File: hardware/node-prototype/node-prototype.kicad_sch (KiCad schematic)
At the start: 0 parts

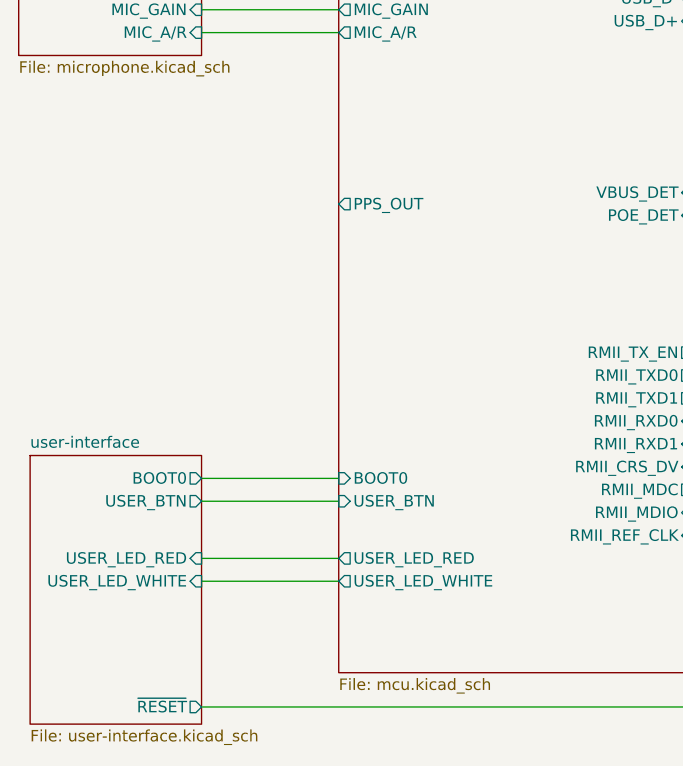
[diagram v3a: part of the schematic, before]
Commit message: Design PPS output, fix LEDs and their resistors
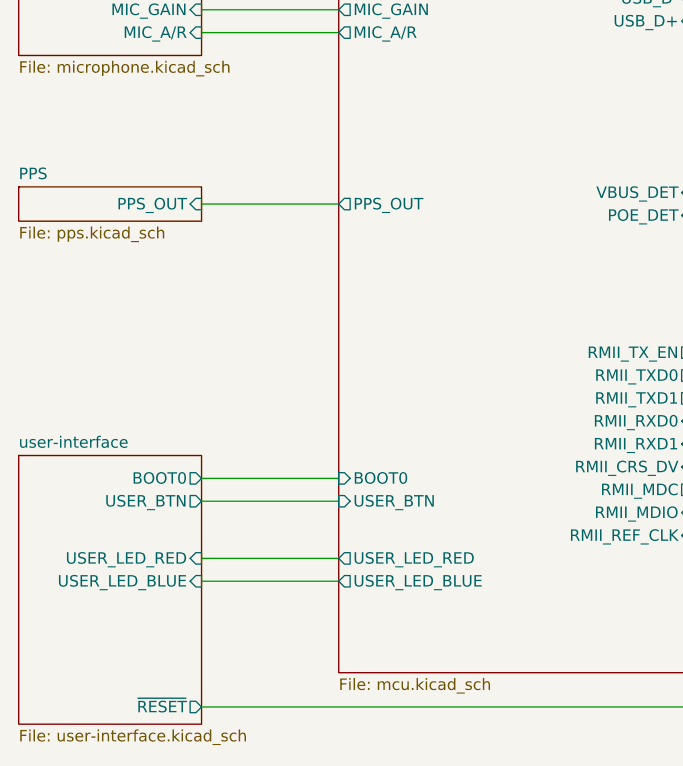
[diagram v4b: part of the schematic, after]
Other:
- added sheet PPS (pps.kicad_sch)
- sheet mcu ports: added USER_LED_BLUE; removed USER_LED_WHITE
- sheet user-interface ports: added USER_LED_BLUE; removed USER_LED_WHITE
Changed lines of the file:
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@@
+    (stroke (width 0) (type default))
+  )
+  (wire (pts (xy 82.55 76.2) (xy 97.79 76.2))
     (stroke (width 0) (type default))
   )
@@
     (effects (font (size 1.27 1.27)) (justify left bottom))
   )
-  (sheet (at 63.5 104.14) (size 19.05 29.845) (fields_autoplaced)
-    (stroke (width 0.1524) (type solid))
-    (fill (color 0 0 0 0.0000))
-    (property "Sheetname" "user-interface" (at 63.5 103.4284 0)
-      (effects (font (size 1.27 1.27)) (justify left bottom))
-    )
-    (property "Sheetfile" "user-interface.kicad_sch" (at 63.5 134.5696 0)
+  (sheet (at 62.23 104.14) (size 20.32 29.845) (fields_autoplaced)
+    (stroke (width 0.1524) (type solid))
+    (fill (color 0 0 0 0.0000))
+    (property "Sheetname" "user-interface" (at 62.23 103.4284 0)
+      (effects (font (size 1.27 1.27)) (justify left bottom))
+    )
+    (property "Sheetfile" "user-interface.kicad_sch" (at 62.23 134.5696 0)
       (effects (font (size 1.27 1.27)) (justify left top))
     )
@@
       (effects (font (size 1.27 1.27)) (justify right))
     )
-    (pin "USER_LED_WHITE" input (at 82.55 118.11 0)
+    (pin "USER_LED_BLUE" input (at 82.55 118.11 0)
       (effects (font (size 1.27 1.27)) (justify right))
     )
@@
     )
   )
+  (sheet (at 62.23 74.295) (size 20.32 3.81) (fields_autoplaced)
+    (stroke (width 0.1524) (type solid))
+    (fill (color 0 0 0 0.0000))
+    (property "Sheetname" "PPS" (at 62.23 73.5834 0)
+      (effects (font (size 1.27 1.27)) (justify left bottom))
+    )
+    (property "Sheetfile" "pps.kicad_sch" (at 62.23 78.6896 0)
+      (effects (font (size 1.27 1.27)) (justify left top))
+    )
+    (pin "PPS_OUT" input (at 82.55 76.2 0)
+      (effects (font (size 1.27 1.27)) (justify right))
+    )
+    (instances
+      (project "node-prototype"
+        (path "/294f7425-8100-4c88-a430-3b04b29ed98a" (page "9"))
+      )
+    )
+  )
   (sheet (at 62.23 46.99) (size 20.32 12.7) (fields_autoplaced)
     (stroke (width 0.1524) (type solid))
@@
       (effects (font (size 1.27 1.27)) (justify right))
     )
-    (pin "USER_LED_WHITE" output (at 97.79 118.11 180)
-      (effects (font (size 1.27 1.27)) (justify left))
-    )
     (pin "USB_D-" bidirectional (at 137.16 53.34 0)
       (effects (font (size 1.27 1.27)) (justify right))
@@
       (effects (font (size 1.27 1.27)) (justify left))
     )
+    (pin "USER_LED_BLUE" output (at 97.79 118.11 180)
+      (effects (font (size 1.27 1.27)) (justify left))
+    )

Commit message: Double check schematic
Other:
- sheet PPS ports: added SYNC_IN0, SYNC_IN1; removed none
- sheet ethernet ports: added CRS_DV, MDC, MDIO, REF_CLK, RXD0, RXD1, TXD0, TXD1, TX_EN; removed RMII_CRS_DV, RMII_MDC, RMII_MDIO, RMII_REF_CLK, RMII_RXD0, RMII_RXD1, RMII_TXD0, RMII_TXD1, RMII_TX_EN
- sheet mcu ports: added SYNC_IN0, SYNC_IN1; removed none
- sheet microphone ports: added AUDIO, A/R, GAIN, ~{SHDN}; removed MIC_AUDIO, MIC_A/R, MIC_GAIN, ~{MIC_SHDN}
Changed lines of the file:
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@@
+    (stroke (width 0) (type default))
+  )
+  (wire (pts (xy 82.55 81.28) (xy 97.79 81.28))
     (stroke (width 0) (type default))
   )
@@
   )
   (wire (pts (xy 82.55 118.11) (xy 97.79 118.11))
+    (stroke (width 0) (type default))
+  )
+  (wire (pts (xy 82.55 78.74) (xy 97.79 78.74))
     (stroke (width 0) (type default))
   )
@@
     )
   )
-  (sheet (at 62.23 74.295) (size 20.32 3.81) (fields_autoplaced)
+  (sheet (at 62.23 74.295) (size 20.32 9.525) (fields_autoplaced)
     (stroke (width 0.1524) (type solid))
     (fill (color 0 0 0 0.0000))
@@
       (effects (font (size 1.27 1.27)) (justify left bottom))
     )
-    (property "Sheetfile" "pps.kicad_sch" (at 62.23 78.6896 0)
+    (property "Sheetfile" "pps.kicad_sch" (at 62.23 84.4046 0)
       (effects (font (size 1.27 1.27)) (justify left top))
     )
@@
       (effects (font (size 1.27 1.27)) (justify right))
     )
+    (pin "SYNC_IN1" output (at 82.55 81.28 0)
+      (effects (font (size 1.27 1.27)) (justify right))
+    )
+    (pin "SYNC_IN0" output (at 82.55 78.74 0)
+      (effects (font (size 1.27 1.27)) (justify right))
+    )
     (instances
       (project "node-prototype"
@@
       (effects (font (size 1.27 1.27)) (justify left top))
     )
-    (pin "MIC_GAIN" input (at 82.55 54.61 0)
-      (effects (font (size 1.27 1.27)) (justify right))
-    )
-    (pin "MIC_AUDIO" output (at 82.55 49.53 0)
-      (effects (font (size 1.27 1.27)) (justify right))
-    )
-    (pin "~{MIC_SHDN}" input (at 82.55 52.07 0)
-      (effects (font (size 1.27 1.27)) (justify right))
-    )
-    (pin "MIC_A{slash}R" input (at 82.55 57.15 0)
+    (pin "A{slash}R" input (at 82.55 57.15 0)
+      (effects (font (size 1.27 1.27)) (justify right))
+    )
+    (pin "AUDIO" output (at 82.55 49.53 0)
+      (effects (font (size 1.27 1.27)) (justify right))
+    )
+    (pin "~{SHDN}" input (at 82.55 52.07 0)
+      (effects (font (size 1.27 1.27)) (justify right))
+    )
+    (pin "GAIN" input (at 82.55 54.61 0)
       (effects (font (size 1.27 1.27)) (justify right))
     )
@@
       (effects (font (size 1.27 1.27)) (justify left top))
     )
-    (pin "RMII_TX_EN" input (at 152.4 92.71 180)
-      (effects (font (size 1.27 1.27)) (justify left))
-    )
-    (pin "RMII_TXD0" input (at 152.4 95.25 180)
-      (effects (font (size 1.27 1.27)) (justify left))
-    )
-    (pin "RMII_TXD1" input (at 152.4 97.79 180)
-      (effects (font (size 1.27 1.27)) (justify left))
-    )
-    (pin "RMII_RXD0" output (at 152.4 100.33 180)
-      (effects (font (size 1.27 1.27)) (justify left))
-    )
-    (pin "RMII_RXD1" output (at 152.4 102.87 180)
-      (effects (font (size 1.27 1.27)) (justify left))
-    )
-    (pin "RMII_CRS_DV" output (at 152.4 105.41 180)
-      (effects (font (size 1.27 1.27)) (justify left))
-    )
-    (pin "RMII_MDC" input (at 152.4 107.95 180)
-      (effects (font (size 1.27 1.27)) (justify left))
-    )
-    (pin "RMII_MDIO" bidirectional (at 152.4 110.49 180)
-      (effects (font (size 1.27 1.27)) (justify left))
-    )
-    (pin "RMII_REF_CLK" output (at 152.4 113.03 180)
-      (effects (font (size 1.27 1.27)) (justify left))
-    )
     (pin "POE_5V" output (at 180.34 93.98 0)
       (effects (font (size 1.27 1.27)) (justify right))
@@
       (effects (font (size 1.27 1.27)) (justify left))
     )
+    (pin "TX_EN" input (at 152.4 92.71 180)
+      (effects (font (size 1.27 1.27)) (justify left))
+    )
+    (pin "REF_CLK" output (at 152.4 113.03 180)
+      (effects (font (size 1.27 1.27)) (justify left))
+    )
+    (pin "MDIO" bidirectional (at 152.4 110.49 180)
+      (effects (font (size 1.27 1.27)) (justify left))
+    )
+    (pin "MDC" input (at 152.4 107.95 180)
+      (effects (font (size 1.27 1.27)) (justify left))
+    )
+    (pin "CRS_DV" output (at 152.4 105.41 180)
+      (effects (font (size 1.27 1.27)) (justify left))
+    )
+    (pin "RXD1" output (at 152.4 102.87 180)
+      (effects (font (size 1.27 1.27)) (justify left))
+    )
+    (pin "RXD0" output (at 152.4 100.33 180)
+      (effects (font (size 1.27 1.27)) (justify left))
+    )
+    (pin "TXD0" input (at 152.4 95.25 180)
+      (effects (font (size 1.27 1.27)) (justify left))
+    )
+    (pin "TXD1" input (at 152.4 97.79 180)
+      (effects (font (size 1.27 1.27)) (justify left))
+    )
     (instances
       (project "node-prototype"
@@
       (effects (font (size 1.27 1.27)) (justify left))
     )
+    (pin "SYNC_IN0" input (at 97.79 78.74 180)
+      (effects (font (size 1.27 1.27)) (justify left))
+    )
+    (pin "SYNC_IN1" input (at 97.79 81.28 180)
+      (effects (font (size 1.27 1.27)) (justify left))
+    )

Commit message: Finish placement
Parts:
- added H1, H2, H3, H4: MountingHole_Pad, MountingHole:MountingHole_3.2mm_M3_Pad_Via, symbol Mechanical:MountingHole_Pad
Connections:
- new net GND: H1.1, H2.1, H3.1, H4.1
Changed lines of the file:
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@@
     (effects (font (size 1.27 1.27)) (justify left bottom))
+  )
+  (symbol (lib_id "power:GND") (at 192.405 151.13 0) (unit 1)
+    (in_bom yes) (on_board yes) (dnp no) (fields_autoplaced)
+    (property "Reference" "#PWR0102" (at 192.405 157.48 0)
+      (effects (font (size 1.27 1.27)) hide)
+    )
+    (property "Value" "GND" (at 192.405 156.21 0)
+      (effects (font (size 1.27 1.27)))
+    )
+    (property "Footprint" "" (at 192.405 151.13 0)
+      (effects (font (size 1.27 1.27)) hide)
+    )
+    (property "Datasheet" "" (at 192.405 151.13 0)
+      (effects (font (size 1.27 1.27)) hide)
+    )
+    (pin "1")
+    (instances
+      (project "node-prototype"
+        (path "/294f7425-8100-4c88-a430-3b04b29ed98a"
+          (reference "#PWR0102") (unit 1)
+        )
+      )
+    )
+  )
+  (symbol (lib_id "Mechanical:MountingHole_Pad") (at 192.405 148.59 0) (unit 1)
+    (in_bom yes) (on_board yes) (dnp no) (fields_autoplaced)
+    (property "Reference" "H1" (at 195.58 146.05 0)
+      (effects (font (size 1.27 1.27)) (justify left))
+    )
+    (property "Value" "MountingHole_Pad" (at 195.58 148.59 0)
+      (effects (font (size 1.27 1.27)) (justify left) hide)
+    )
+    (property "Footprint" "MountingHole:MountingHole_3.2mm_M3_Pad_Via" (at 192.405 148.59 0)
+      (effects (font (size 1.27 1.27)) hide)
+    )
+    (property "Datasheet" "~" (at 192.405 148.59 0)
+      (effects (font (size 1.27 1.27)) hide)
+    )
+    (pin "1")
+    (instances
+      (project "node-prototype"
+        (path "/294f7425-8100-4c88-a430-3b04b29ed98a"
+          (reference "H1") (unit 1)
+        )
+      )
+    )
+  )
+  (symbol (lib_id "Mechanical:MountingHole_Pad") (at 223.52 148.59 0) (unit 1)
+    (in_bom yes) (on_board yes) (dnp no) (fields_autoplaced)
+    (property "Reference" "H4" (at 226.695 146.05 0)
+      (effects (font (size 1.27 1.27)) (justify left))
+    )
+    (property "Value" "MountingHole_Pad" (at 226.695 148.59 0)
+      (effects (font (size 1.27 1.27)) (justify left) hide)
+    )
+    (property "Footprint" "MountingHole:MountingHole_3.2mm_M3_Pad_Via" (at 223.52 148.59 0)
+      (effects (font (size 1.27 1.27)) hide)
+    )
+    (property "Datasheet" "~" (at 223.52 148.59 0)
+      (effects (font (size 1.27 1.27)) hide)
+    )
+    (pin "1")
+    (instances
+      (project "node-prototype"
+        (path "/294f7425-8100-4c88-a430-3b04b29ed98a"
+          (reference "H4") (unit 1)
+        )
+      )
+    )
+  )
+  (symbol (lib_id "Mechanical:MountingHole_Pad") (at 213.36 148.59 0) (unit 1)
+    (in_bom yes) (on_board yes) (dnp no) (fields_autoplaced)
+    (property "Reference" "H3" (at 216.535 146.05 0)
+      (effects (font (size 1.27 1.27)) (justify left))
+    )
+    (property "Value" "MountingHole_Pad" (at 216.535 148.59 0)
+      (effects (font (size 1.27 1.27)) (justify left) hide)
+    )
+    (property "Footprint" "MountingHole:MountingHole_3.2mm_M3_Pad_Via" (at 213.36 148.59 0)
+      (effects (font (size 1.27 1.27)) hide)
+    )
+    (property "Datasheet" "~" (at 213.36 148.59 0)
+      (effects (font (size 1.27 1.27)) hide)
+    )
+    (pin "1")
+    (instances
+      (project "node-prototype"
+        (path "/294f7425-8100-4c88-a430-3b04b29ed98a"
+          (reference "H3") (unit 1)
+        )
+      )
+    )
+  )
+  (symbol (lib_id "power:GND") (at 223.52 151.13 0) (unit 1)
+    (in_bom yes) (on_board yes) (dnp no) (fields_autoplaced)
+    (property "Reference" "#PWR0105" (at 223.52 157.48 0)
+      (effects (font (size 1.27 1.27)) hide)
+    )
+    (property "Value" "GND" (at 223.52 156.21 0)
+      (effects (font (size 1.27 1.27)))
+    )
+    (property "Footprint" "" (at 223.52 151.13 0)
+      (effects (font (size 1.27 1.27)) hide)
+    )
+    (property "Datasheet" "" (at 223.52 151.13 0)
+      (effects (font (size 1.27 1.27)) hide)
+    )
+    (pin "1")
+    (instances
+      (project "node-prototype"
+        (path "/294f7425-8100-4c88-a430-3b04b29ed98a"
+          (reference "#PWR0105") (unit 1)
+        )
+      )
+    )
+  )
+  (symbol (lib_id "power:GND") (at 213.36 151.13 0) (unit 1)
+    (in_bom yes) (on_board yes) (dnp no) (fields_autoplaced)
+    (property "Reference" "#PWR0104" (at 213.36 157.48 0)
+      (effects (font (size 1.27 1.27)) hide)
+    )
+    (property "Value" "GND" (at 213.36 156.21 0)
+      (effects (font (size 1.27 1.27)))
+    )
+    (property "Footprint" "" (at 213.36 151.13 0)
+      (effects (font (size 1.27 1.27)) hide)
+    )
+    (property "Datasheet" "" (at 213.36 151.13 0)
+      (effects (font (size 1.27 1.27)) hide)
+    )
+    (pin "1")
+    (instances
+      (project "node-prototype"
+        (path "/294f7425-8100-4c88-a430-3b04b29ed98a"
+          (reference "#PWR0104") (unit 1)
+        )
+      )
+    )
+  )
+  (symbol (lib_id "power:GND") (at 202.565 151.13 0) (unit 1)
+    (in_bom yes) (on_board yes) (dnp no) (fields_autoplaced)
+    (property "Reference" "#PWR0103" (at 202.565 157.48 0)
+      (effects (font (size 1.27 1.27)) hide)
+    )
+    (property "Value" "GND" (at 202.565 156.21 0)
+      (effects (font (size 1.27 1.27)))
+    )
+    (property "Footprint" "" (at 202.565 151.13 0)
+      (effects (font (size 1.27 1.27)) hide)
+    )
+    (property "Datasheet" "" (at 202.565 151.13 0)
+      (effects (font (size 1.27 1.27)) hide)
+    )
+    (pin "1")
+    (instances
+      (project "node-prototype"
+        (path "/294f7425-8100-4c88-a430-3b04b29ed98a"
+          (reference "#PWR0103") (unit 1)
+        )
+      )
+    )
+  )
+  (symbol (lib_id "Mechanical:MountingHole_Pad") (at 202.565 148.59 0) (unit 1)
+    (in_bom yes) (on_board yes) (dnp no) (fields_autoplaced)
+    (property "Reference" "H2" (at 205.74 146.05 0)
+      (effects (font (size 1.27 1.27)) (justify left))
+    )
+    (property "Value" "MountingHole_Pad" (at 205.74 148.59 0)
+      (effects (font (size 1.27 1.27)) (justify left) hide)
+    )
+    (property "Footprint" "MountingHole:MountingHole_3.2mm_M3_Pad_Via" (at 202.565 148.59 0)
+      (effects (font (size 1.27 1.27)) hide)
+    )
+    (property "Datasheet" "~" (at 202.565 148.59 0)
+      (effects (font (size 1.27 1.27)) hide)
+    )
+    (pin "1")
+    (instances
+      (project "node-prototype"
+        (path "/294f7425-8100-4c88-a430-3b04b29ed98a"
+          (reference "H2") (unit 1)
+        )
+      )
+    )
   )
   (sheet (at 62.23 104.14) (size 20.32 29.845) (fields_autoplaced)

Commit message: prepare for production
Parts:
- H1, H2, H3, H4: now left out of the parts list
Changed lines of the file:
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@@
   )
   (symbol (lib_id "Mechanical:MountingHole_Pad") (at 192.405 148.59 0) (unit 1)
-    (in_bom yes) (on_board yes) (dnp no) (fields_autoplaced)
+    (in_bom no) (on_board yes) (dnp no) (fields_autoplaced)
     (property "Reference" "H1" (at 195.58 146.05 0)
       (effects (font (size 1.27 1.27)) (justify left))
@@
   )
   (symbol (lib_id "Mechanical:MountingHole_Pad") (at 223.52 148.59 0) (unit 1)
-    (in_bom yes) (on_board yes) (dnp no) (fields_autoplaced)
+    (in_bom no) (on_board yes) (dnp no) (fields_autoplaced)
     (property "Reference" "H4" (at 226.695 146.05 0)
       (effects (font (size 1.27 1.27)) (justify left))
@@
   )
   (symbol (lib_id "Mechanical:MountingHole_Pad") (at 213.36 148.59 0) (unit 1)
-    (in_bom yes) (on_board yes) (dnp no) (fields_autoplaced)
+    (in_bom no) (on_board yes) (dnp no) (fields_autoplaced)
     (property "Reference" "H3" (at 216.535 146.05 0)
       (effects (font (size 1.27 1.27)) (justify left))
@@
   )
   (symbol (lib_id "Mechanical:MountingHole_Pad") (at 202.565 148.59 0) (unit 1)
-    (in_bom yes) (on_board yes) (dnp no) (fields_autoplaced)
+    (in_bom no) (on_board yes) (dnp no) (fields_autoplaced)
     (property "Reference" "H2" (at 205.74 146.05 0)
       (effects (font (size 1.27 1.27)) (justify left))
